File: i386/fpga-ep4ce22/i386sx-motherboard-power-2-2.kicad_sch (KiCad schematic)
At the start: 49 parts, among them J2 PJ-063AH 12V, U10 TLV62569DBVR VCCAUX, U7 TPS5430DDAR 12->5V, U9 TPS62130RGTR VCCINT

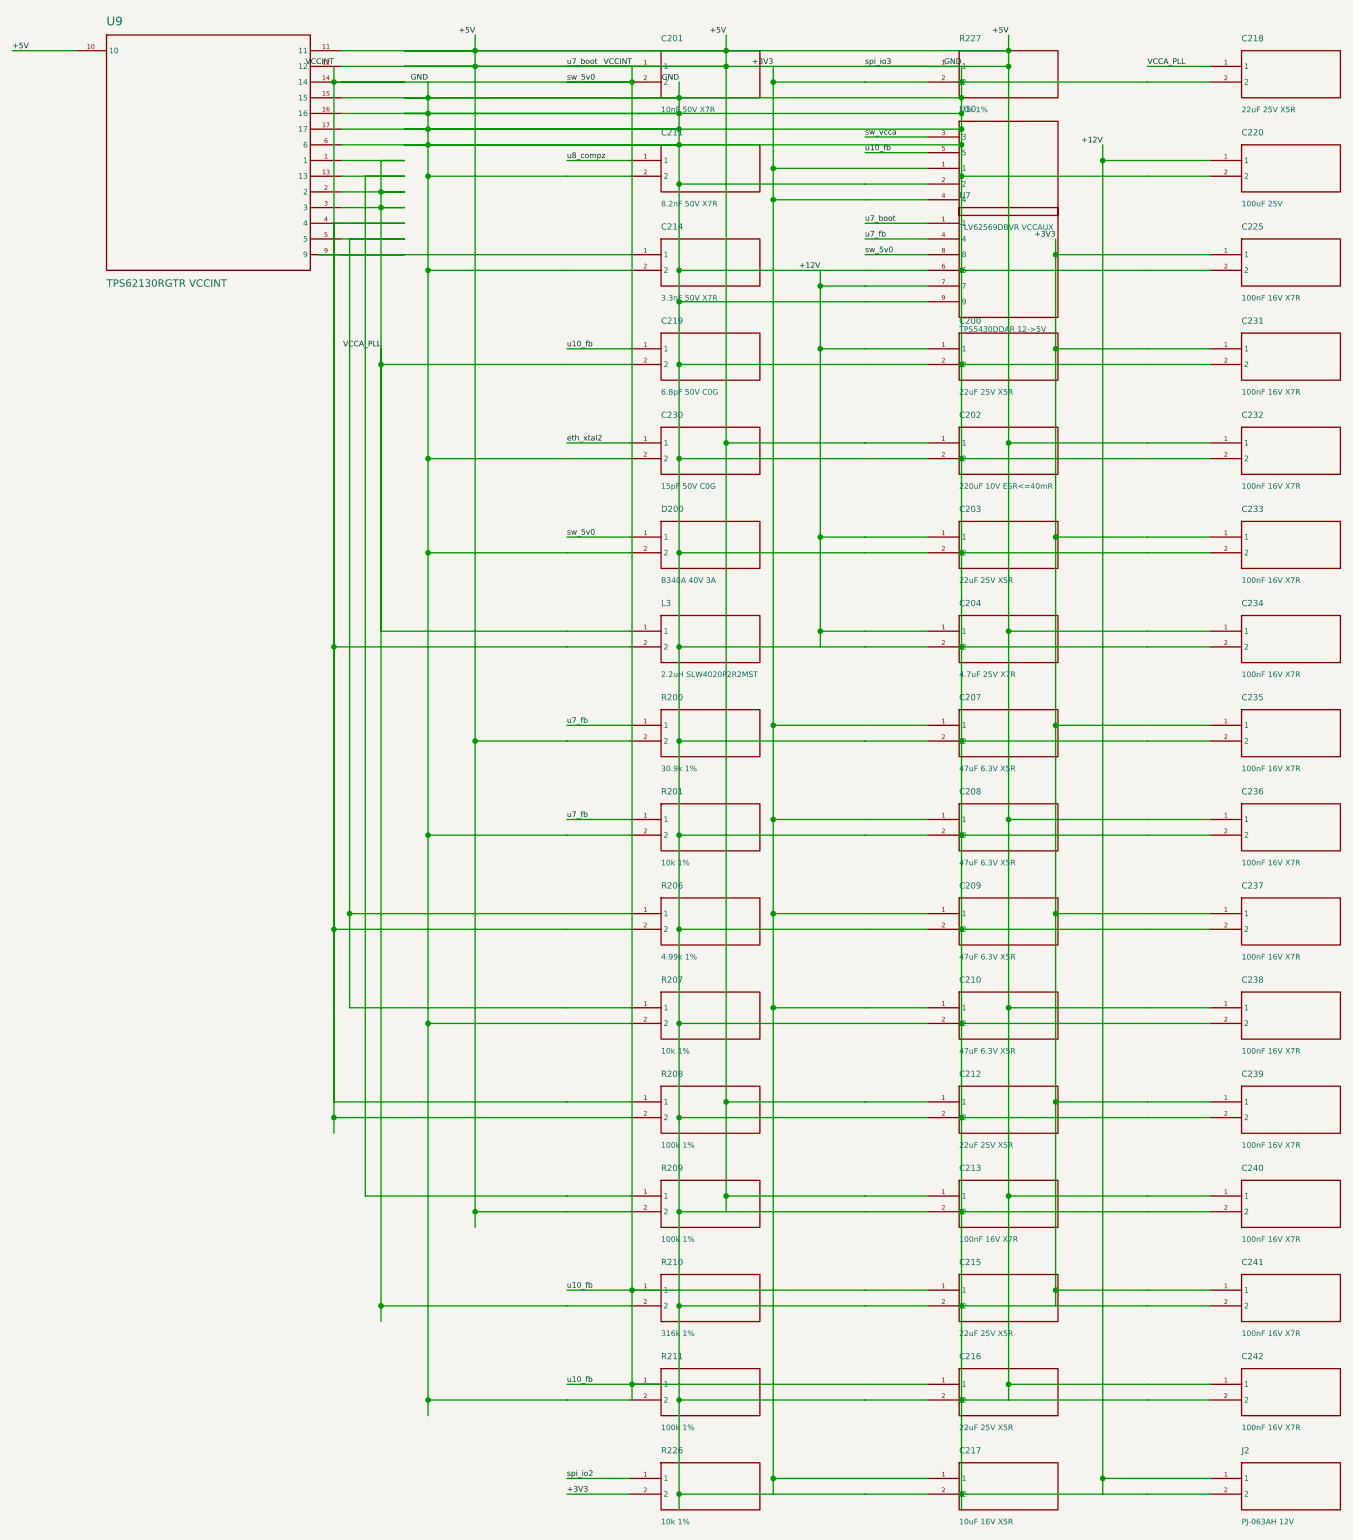
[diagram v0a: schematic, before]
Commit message: Publish the motherboards' KiCad files
From socket3@c0f6464 socket7@9205469 socket370@524f5b1 i386@bea926c
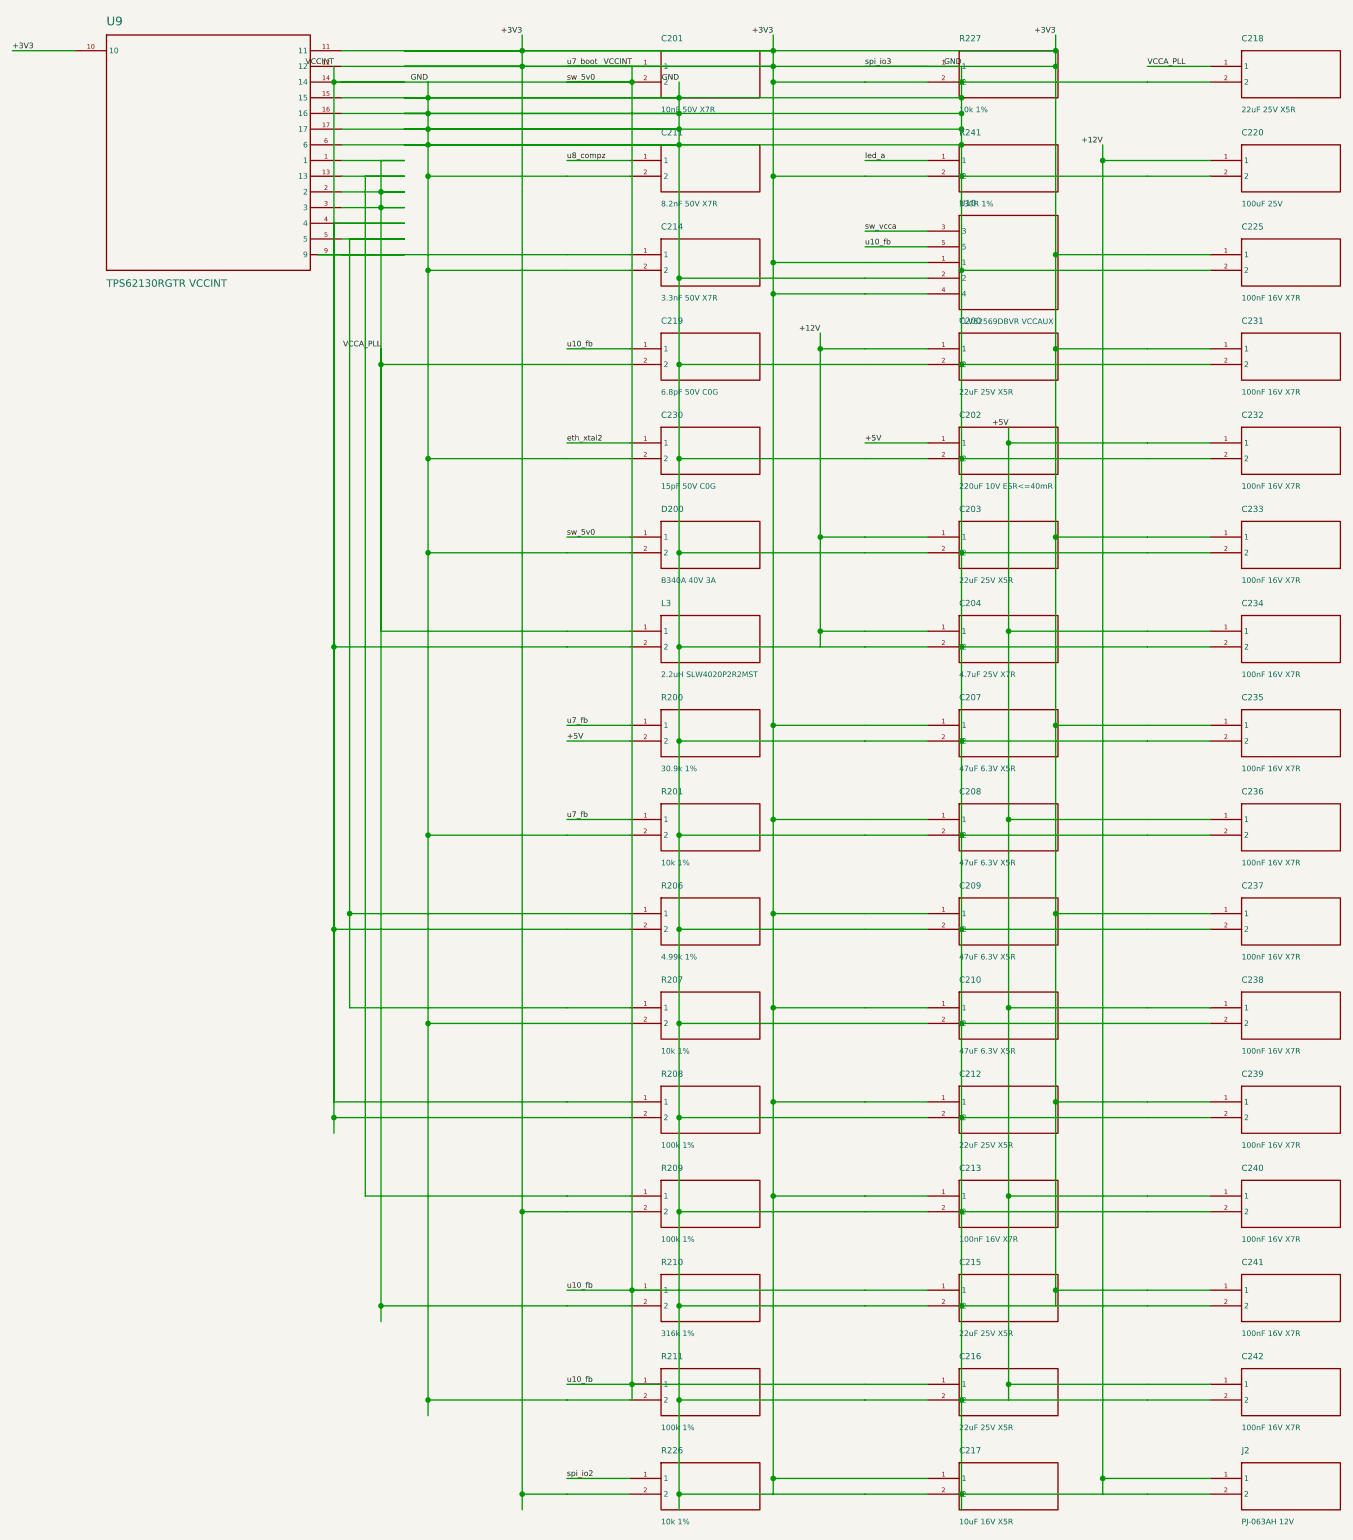
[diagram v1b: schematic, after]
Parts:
- removed U7: TPS5430DDAR 12->5V, symbol gen:S6_0s
- added R241: 330R 1%, symbol gen:S2_0s
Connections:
- net +12V: no longer C200.2, C201.1, C201.2, C202.1, C202.2, C203.2, C204.2, C207.1, C207.2, C208.1, C208.2, C209.1, C209.2, C210.1, C210.2, C211.2, C212.1, C212.2, C213.1, C213.2, C214.2, C215.1, C215.2, C216.1, C216.2, C217.1, C217.2, C218.2, C220.2, C225.1, C225.2, C230.2, C231.1, C231.2, C232.1, C232.2, C233.1, C233.2, C234.1, C234.2, C235.1, C235.2, C236.1, C236.2, C237.1, C237.2, C238.1, C238.2, C239.1, C239.2, C240.1, C240.2, C241.1, C241.2, C242.1, C242.2, D200.1, D200.2, J2.2, L3.2, R200.2, R201.2, R206.2, R207.2, R208.1, R208.2, R209.2, R211.2, R226.2, R227.1, R227.2, U10.1, U10.2, U10.4, U9.10, U9.11, U9.12, U9.14, U9.15, U9.16, U9.17, U9.4, U9.6
- new net +3V3: C200.2, C201.1, C201.2, C202.2, C203.2, C204.2, C207.1, C207.2, C208.1, C208.2, C209.1, C209.2, C210.1, C210.2, C211.2, C212.1, C212.2, C213.1, C213.2, C214.2, C215.1, C215.2, C216.1, C216.2, C217.1, C217.2, C218.2, C220.2, C225.1, C225.2, C230.2, C231.1, C231.2, C232.2, C233.1, C233.2, C234.2, C235.1, C235.2, C236.2, C237.1, C237.2, C238.2, C239.1, C239.2, C240.2, C241.1, C241.2, C242.2, D200.1, D200.2, J2.2, L3.2, R201.2, R206.2, R207.2, R208.1, R208.2, R209.2, R211.2, R226.2, R227.1, R227.2, R241.2, U10.1, U10.2, U10.4, U9.10, U9.11, U9.12, U9.14, U9.15, U9.16, U9.17, U9.4, U9.6
- new net +5V: C202.1, C232.1, C234.1, C236.1, C238.1, C240.1, C242.1, R200.2
- new net led_a: R241.1
